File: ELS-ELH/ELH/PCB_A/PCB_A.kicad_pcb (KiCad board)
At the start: 2 copper layers, 95 x 95 mm, 40 parts, among them J1 Pressure Transducer Input, J2 Conn_01x09_Pin, J3 Conn_01x20_Pin, J4 Conn_01x20_Pin, Q1 IRLZ44N, Q2 IRLZ44N, Q4 IRLZ44N, Q6 IRLZ44N

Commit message: PCB B Advanced
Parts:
- J3, J4: footprint Connector_PinSocket_2.54mm:PinSocket_1x20_P2.54mm_Vertical -> Connector_PinHeader_2.54mm:PinHeader_1x20_P2.54mm_Vertical; moved to B.Cu
- moved J3 48.2 mm to (24.1, -40.0)
- moved J4 48.2 mm to (24.1, 40.0)

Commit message: Update of 3D Models
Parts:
- removed J1: Pressure Transducer Input, TerminalBlock:TerminalBlock_MaiXu_MX126-5.0-03P_1x03_P5.00mm
- removed J2: Conn_01x09_Pin, Connector_Hirose:Hirose_DF13-09P-1.25DSA_1x09_P1.25mm_Vertical
- J3, J4: footprint Connector_PinHeader_2.54mm:PinHeader_1x20_P2.54mm_Vertical -> Connector_PinSocket_2.54mm:PinSocket_1x20_P2.54mm_Vertical
- R1, R10, R11, R16, R18, R19, R2, R20, R3, R6, R8, R9: moved to B.Cu
- moved R20 100.5 mm to (-17.2, 2.55), turned to 180 degrees
- moved R18 100.5 mm to (-17.2, -5.55), turned to 180 degrees
- moved R19 100.5 mm to (-17.2, -1.50), turned to 180 degrees
- moved R10 85.8 mm to (25.8, -1.00), turned to 180 degrees
- moved R11 85.8 mm to (25.8, 3.05), turned to 180 degrees
- moved R9 85.8 mm to (25.8, -5.05), turned to 180 degrees
- moved C3 77.6 mm to (33.8, -35.0)
- moved C1 72.0 mm to (27.0, 17.5), turned to 90 degrees
- moved R16 58.8 mm to (10.0, 31.1), turned to 90 degrees
- moved R8 50.1 mm to (6.15, 23.2), turned to -90 degrees
- moved R6 45.8 mm to (2.10, 23.2), turned to -90 degrees
- moved R3 41.9 mm to (-1.95, 23.2), turned to -90 degrees
- moved R2 38.4 mm to (-6.00, 23.2), turned to -90 degrees
- moved R1 35.5 mm to (-10.1, 23.2), turned to -90 degrees
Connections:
- Regulator3 pad 3: Net-(Bornera2-Pin_1) -> GND
- Regulator3 pad 4: Net-(Bornera2-Pin_2) -> +5V

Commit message: advances
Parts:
- moved Bornera1 74.8 mm to (-33.5, -16.6), turned to -90 degrees
- moved Bornera7 67.8 mm to (33.5, -6.45), turned to 90 degrees
- moved R8 54.6 mm to (49.6, -9.95), turned to 0 degrees
- moved BOOST1 48.3 mm to (22.3, 37.8), turned to 180 degrees
- moved R16 37.0 mm to (-17.2, 6.00), turned to 180 degrees
- moved R1 34.1 mm to (-23.8, -8.00), turned to 0 degrees
- moved R19 33.1 mm to (-10.0, 30.8), turned to 90 degrees
- moved R6 31.9 mm to (17.9, -4.50), turned to 0 degrees
- moved R9 31.7 mm to (57.5, -6.50)
- moved R11 29.0 mm to (17.5, 30.8), turned to 90 degrees
- moved Bornera4 23.0 mm to (33.5, 16.6)
- moved R20 20.9 mm to (-14.0, 23.2), turned to -90 degrees
- moved R3 14.9 mm to (13.0, 23.2)
- moved D1 10.2 mm to (37.5, 21.5), turned to 180 degrees
- moved Q1 9.64 mm to (35.5, 26.5), turned to 180 degrees
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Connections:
- net /Ch_B_mosfet_1 renamed /Ch_C_mosfet_1
- R6 pad 1: /Ch_B_mosfet_2 -> /Ch_C_mosfet_2
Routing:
- net Net-(Bornera4-Pin_1): track 0.00 -> 80.4 mm
- net /Ch_D_mosfet_2: track 0.00 -> 62.5 mm
- net Net-(Bornera5-Pin_1): track 0.00 -> 44.9 mm
- net Net-(BOOST1-IN-): track 0.00 -> 43.9 mm
- net Net-(BOOST1-IN+): track 0.00 -> 41.0 mm
- net +12V: track 0.00 -> 40.9 mm
- net Net-(Q1-G): track 0.00 -> 36.9 mm
- net Net-(Bornera1-Pin_1): track 0.00 -> 35.9 mm
- net Net-(Bornera1-Pin_2): track 0.00 -> 35.1 mm
- net /Ch_C_mosfet_2: track 0.00 -> 32.5 mm
- net Net-(Q6-G): track 0.00 -> 31.1 mm
- net Net-(Q4-G): track 0.00 -> 18.9 mm
- net Net-(Q2-G): track 0.00 -> 16.9 mm
- net Net-(Q1-S): track 0.00 -> 9.05 mm
- net Net-(Q2-D): track 0.00 -> 6.49 mm

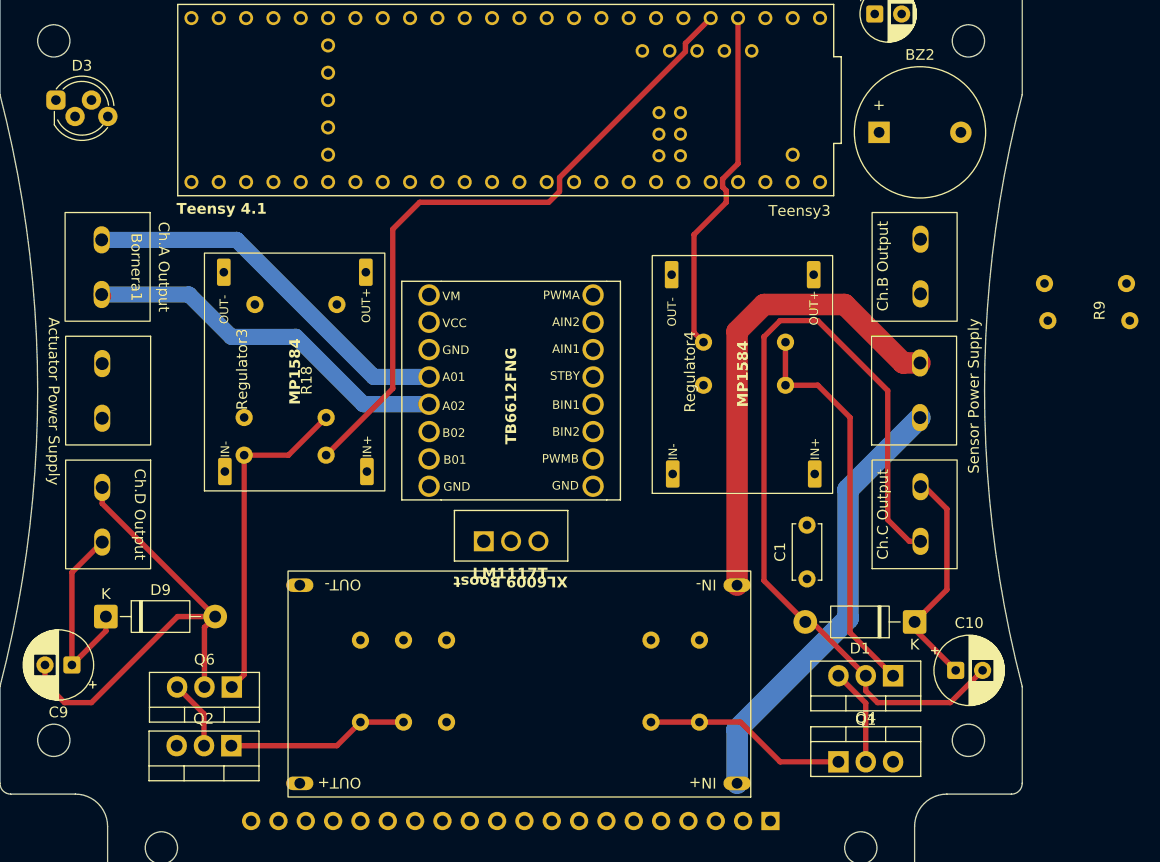
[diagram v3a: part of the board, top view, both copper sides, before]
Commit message: Updates
The boost component was replaced, capacitors were added for the regulator, and the power supply voltage for the expansion module was changed
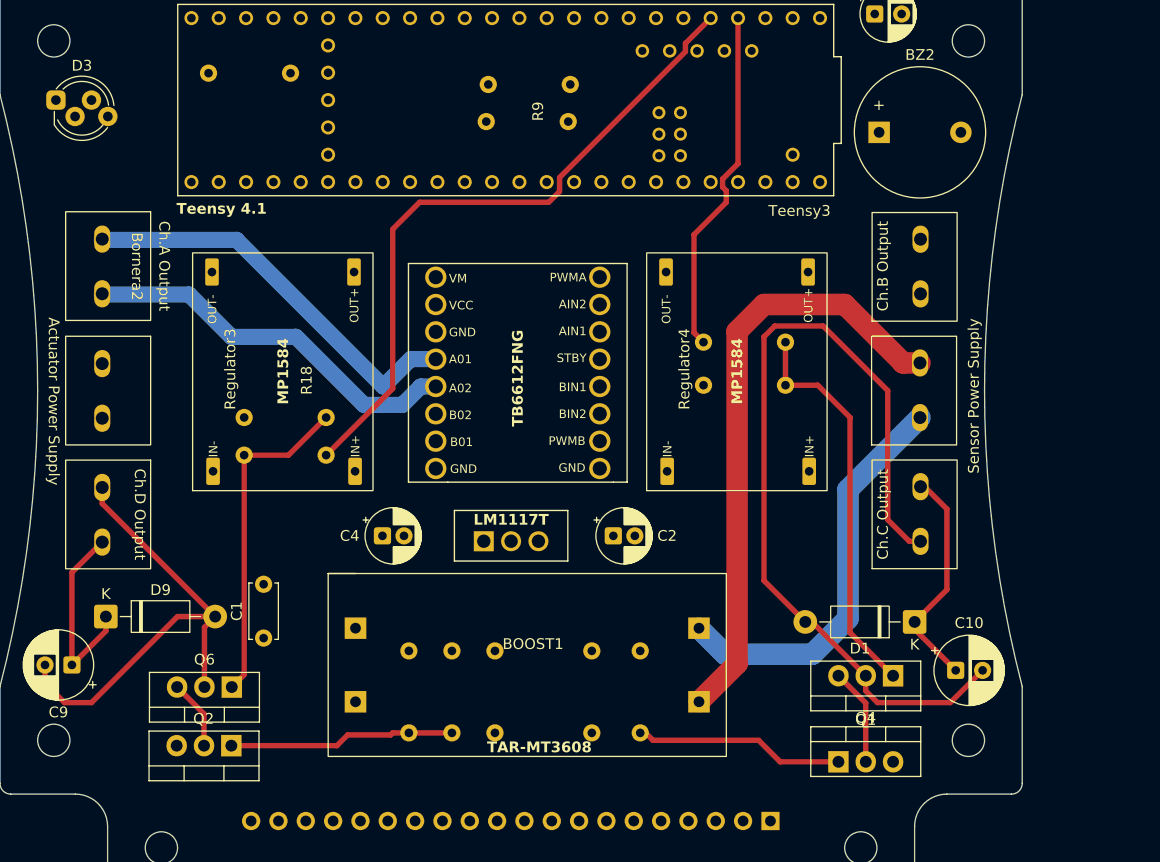
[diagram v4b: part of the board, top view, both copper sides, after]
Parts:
- removed Bornera1: Ch.A Output, ELH_Library:Bornera 2P
- added Bornera2: Ch.A Output, ELH_Library:Bornera 2P, F.Cu at (-33.5, -16.6)
- added C2: 10uF, Capacitor_THT:CP_Radial_D5.0mm_P2.00mm, F.Cu at (9.50, 13.5)
- added C4: 10uF, Capacitor_THT:CP_Radial_D5.0mm_P2.00mm, F.Cu at (-12.0, 13.5)
- BOOST1: value XL6009 -> TAR-MT3608; footprint ELH_Library:XL6009 Boost -> ELH_Library:TAR-MT3608
- moved R9 55.4 mm to (5.31, -25.0)
- moved R8 54.9 mm to (-2.12, -28.4)
- moved C1 50.8 mm to (-23.0, 23.0)
- moved BOOST1 44.4 mm to (-17.0, 17.0), turned to 0 degrees
- moved R1 21.9 mm to (-28.1, -29.5)
- moved R11 5.59 mm to (12.0, 31.8)
- moved R3 5.59 mm to (7.50, 24.2)
- moved R19 4.61 mm to (-5.50, 31.8)
- moved R2 4.61 mm to (-1.50, 24.2)
- moved R20 4.61 mm to (-9.50, 24.2)
- moved Driver_DC2 1.76 mm to (0.62, -1.65)
- moved Regulator3 1.10 mm to (-29.6, 9.30)
- moved Regulator4 0.57 mm to (12.6, 9.30)
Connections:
- Regulator1 pad 1: +5V -> GND
- Regulator1 pad 3: GND -> +5V
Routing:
- net Net-(BOOST1-IN-): track 43.9 -> 56.2 mm
- net Net-(Q2-G): track 16.9 -> 21.0 mm
- net Net-(BOOST1-IN+): track 41.0 -> 37.7 mm
- net Net-(Bornera2-Pin_1): track 35.9 -> 37.7 mm
- net Net-(Bornera2-Pin_2): track 35.1 -> 36.0 mm
- net Net-(Q4-G): track 18.9 -> 19.5 mm

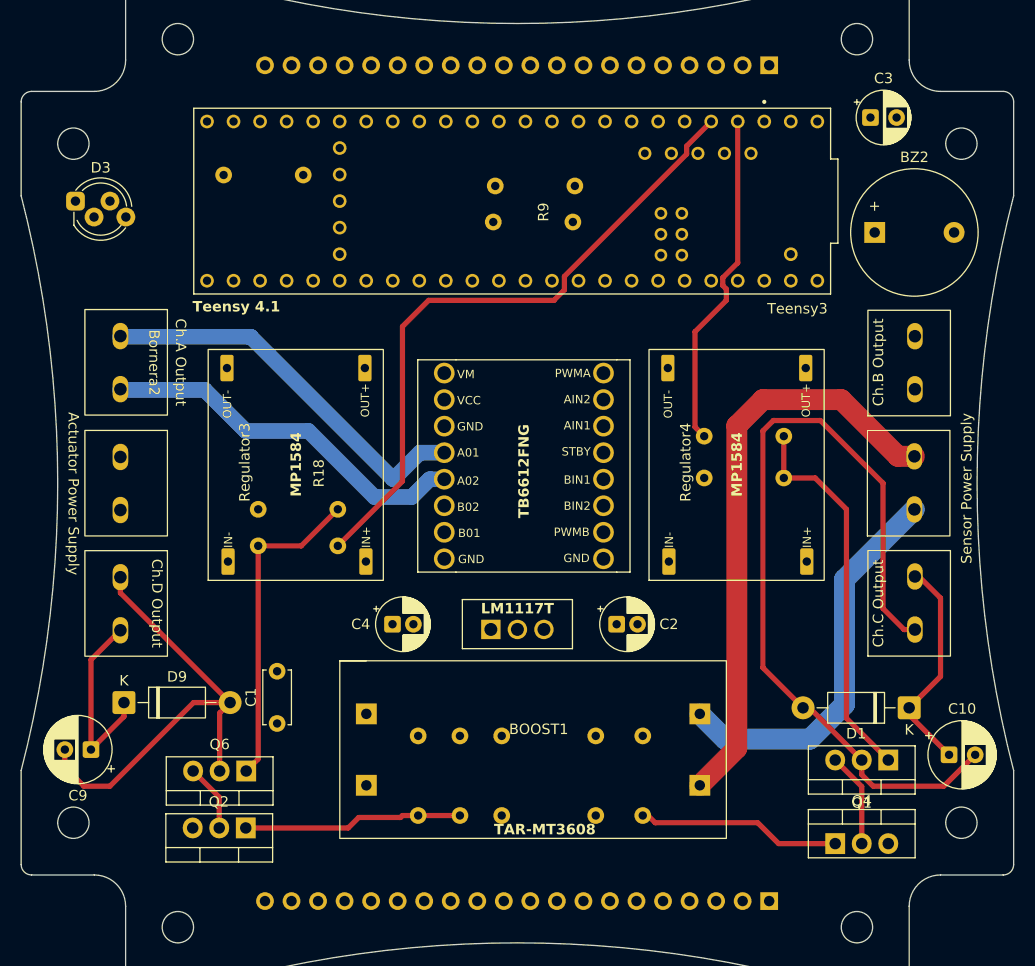
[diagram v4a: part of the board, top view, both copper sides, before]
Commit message: preliminary PCB A connections
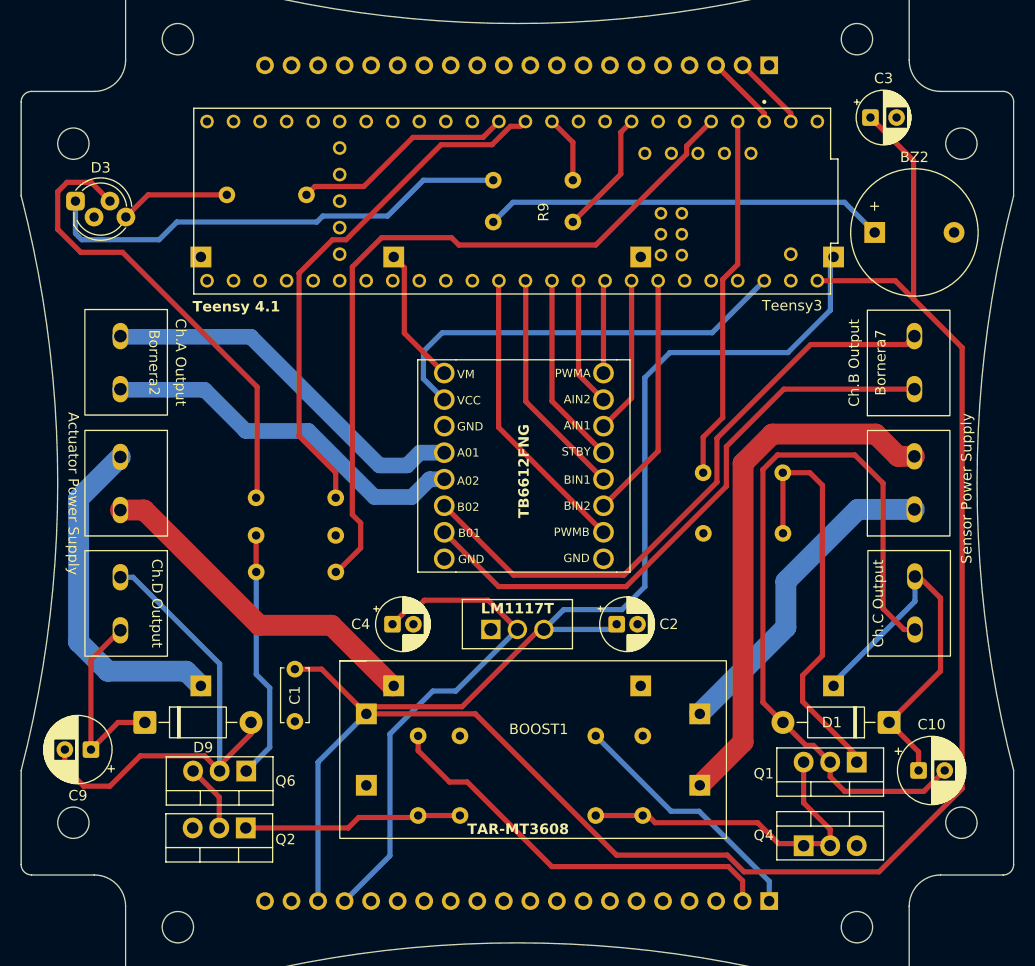
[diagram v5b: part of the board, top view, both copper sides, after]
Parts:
- Regulator3, Regulator4: value MP1584 -> LM2596; footprint ELH_Library:MP1584 -> ELH_Library:LM2596; moved to B.Cu
- moved Regulator3 62.2 mm to (31.5, 20.7)
- moved R2 32.7 mm to (-25.0, 1.40), turned to 0 degrees
- moved Regulator4 25.8 mm to (-10.6, 20.7)
- moved R18 8.21 mm to (-25.0, 5.00), turned to 0 degrees
- moved R10 5.30 mm to (25.4, 4.80)
- moved R6 3.50 mm to (17.8, -1.00)
- moved C10 3.28 mm to (38.4, 27.5)
- moved Q1 3.03 mm to (32.5, 26.7)
- moved Q4 3.03 mm to (27.4, 34.7)
- moved D9 2.76 mm to (-35.7, 22.9)
- moved R16 2.51 mm to (-17.4, 8.50)
- moved D1 2.38 mm to (35.6, 22.9)
- moved R1 1.93 mm to (-27.8, -27.6)
- moved C1 1.71 mm to (-21.3, 22.8)
- moved R8 0.58 mm to (-2.31, -29.0)
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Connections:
- J3 pad 1: unconnected-(J3-Pin_1-Pad1) -> GND
- J3 pad 2: unconnected-(J3-Pin_2-Pad2) -> /UART1_TX_1
- J3 pad 3: unconnected-(J3-Pin_3-Pad3) -> /UART1_RX_1
- J4 pad 1: unconnected-(J4-Pin_1-Pad1) -> /Ch_C_mosfet_1
- J4 pad 17: unconnected-(J4-Pin_17-Pad17) -> +3V3
- J4 pad 18: unconnected-(J4-Pin_18-Pad18) -> +5V
- J4 pad 2: unconnected-(J4-Pin_2-Pad2) -> /Ch_D_mosfet_1
- Teensy3 pad 14: /PWMA -> /PWMB
- Teensy3 pad 15: /AIN1 -> /BIN1
- Teensy3 pad 16: /AIN2 -> /STBY
- Teensy3 pad 17: /PWMB -> /AIN2
- Teensy3 pad 18: /BIN1 -> /PWMA
- Teensy3 pad 19: /BIN2 -> /AIN1
- Teensy3 pad 20: /STBY -> /BIN2
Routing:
- net +5V: track 0.00 -> 258.0 mm
- net Net-(Bornera7-Pin_2): track 0.00 -> 59.7 mm
- net Net-(Bornera7-Pin_1): track 0.00 -> 57.2 mm
- net /LED5: track 0.00 -> 50.6 mm
- net +3V3: track 0.00 -> 48.2 mm
- net Net-(D3-GA): track 0.00 -> 45.7 mm
- net Net-(D3-RA): track 0.00 -> 45.7 mm
- net +3.3VA: track 0.00 -> 40.9 mm
- net /Ch_D_mosfet_1: track 0.00 -> 39.6 mm
- net Net-(BZ2-+): track 0.00 -> 38.5 mm
- net Net-(Bornera3-Pin_1): track 0.00 -> 33.1 mm
- net Net-(Bornera3-Pin_2): track 0.00 -> 32.8 mm
- net /PWMB: track 0.00 -> 28.3 mm
- net +12V: track 40.9 -> 68.8 mm
- net /Ch_C_mosfet_1: track 0.00 -> 24.3 mm
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
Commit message: PCB A advances
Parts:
- added BOOST2: TAR-MT3608, ELH_Library:TAR-MT3608, F.Cu at (0.54, 21.1)
- added Bornera1: Camera Connection, ELH_Library:Bornera 2P, F.Cu at (-34.0, 8.10)
- added Bornera8: Camera Power Supply, ELH_Library:Bornera 2P, F.Cu at (33.7, -13.0)
- added J1: Conn_01x08_Pin, Connector_PinSocket_2.54mm:PinSocket_1x08_P2.54mm_Vertical, F.Cu at (-8.94, 9.70)
- J3, R9: moved to F.Cu
- moved C3 62.4 mm to (-24.3, -12.2)
- moved Regulator4 46.1 mm to (-32.5, -19.8), turned to -90 degrees
- moved C1 35.8 mm to (-13.3, -12.1), turned to 180 degrees
- moved D1 34.9 mm to (13.3, -3.90), turned to 0 degrees
- moved R6 34.7 mm to (20.1, 33.6), turned to 90 degrees
- moved C9 33.5 mm to (-14.8, 4.45)
- moved C4 33.0 mm to (21.0, 15.3), turned to 180 degrees
- moved Q2 31.6 mm to (-23.3, 1.50)
- moved R2 30.9 mm to (-26.1, -29.5)
- moved R9 30.8 mm to (30.9, -7.96), turned to -90 degrees
- moved C2 30.6 mm to (-21.0, 15.3), turned to 180 degrees
- moved Q4 28.3 mm to (15.8, 8.90)
- moved Q1 27.8 mm to (20.9, 1.50)
- moved D9 27.4 mm to (-30.1, -3.90)
- moved R16 25.0 mm to (-15.7, 33.5), turned to 90 degrees
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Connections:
- BOOST1 pad 2: Net-(BOOST1-IN-) -> GND
- Bornera3 pad 1: Net-(Bornera3-Pin_2) -> GND
- Bornera6 pad 2: Net-(BOOST1-IN-) -> GND
- Driver_DC2 pad 2: +3.3VA -> +3V3
- J3 pad 3: /UART1_RX_1 -> /UART1_TX_1
- J3 pad 4: unconnected-(J3-Pin_4-Pad4) -> /UART1_TX_1
- J3 pad 5: unconnected-(J3-Pin_5-Pad5) -> /UART1_RX_1
- J3 pad 6: unconnected-(J3-Pin_6-Pad6) -> /UART1_RX_1
- J3 pad 7: unconnected-(J3-Pin_7-Pad7) -> /UART1_RX_1
- J4 pad 1: /Ch_C_mosfet_1 -> unconnected-(J4-Pin_1-Pad1)
- J4 pad 13: unconnected-(J4-Pin_13-Pad13) -> +3V3
- J4 pad 14: unconnected-(J4-Pin_14-Pad14) -> +5V
- J4 pad 17: +3V3 -> unconnected-(J4-Pin_17-Pad17)
- J4 pad 18: +5V -> /Ch_D_mosfet_1
- J4 pad 19: unconnected-(J4-Pin_19-Pad19) -> /Ch_D_mosfet_1
- J4 pad 2: /Ch_D_mosfet_1 -> unconnected-(J4-Pin_2-Pad2)
- J4 pad 20: unconnected-(J4-Pin_20-Pad20) -> /Ch_D_mosfet_1
- J4 pad 7: unconnected-(J4-Pin_7-Pad7) -> /Ch_C_mosfet_1
- J4 pad 8: unconnected-(J4-Pin_8-Pad8) -> /Ch_C_mosfet_1
- J4 pad 9: unconnected-(J4-Pin_9-Pad9) -> /Ch_C_mosfet_1
- Regulator4 pad 1: Net-(Bornera3-Pin_2) -> GND
- Teensy3 pad 1: /UART1_RX_1 -> unconnected-(Teensy3-TX1-Pad1)
- Teensy3 pad 11: /LED6 -> /LED4
- Teensy3 pad 13: unconnected-(Teensy3-SCK-Pad13) -> /LPWM
- Teensy3 pad 2: /Ch_C_mosfet_2 -> unconnected-(Teensy3-OUT2-Pad2)
- Teensy3 pad 22: unconnected-(Teensy3-A8-Pad22) -> /Ch_C_mosfet_2
- Teensy3 pad 3: /Ch_D_mosfet_2 -> unconnected-(Teensy3-LRCLK2-Pad3)
- Teensy3 pad 3.3V_1: +3.3VA -> +3V3
- Teensy3 pad 3.3V_2: +3.3VA -> +3V3
- Teensy3 pad 36: unconnected-(Teensy3-CS2-Pad36) -> /Ch_D_mosfet_2
- Teensy3 pad 4: unconnected-(Teensy3-BCLK2-Pad4) -> /UART1_RX_1
- Teensy3 pad 41: unconnected-(Teensy3-A17-Pad41) -> /RPWM
- Teensy3 pad 9: /LED4 -> /LED6
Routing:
- net +3V3: track 48.2 -> 253.5 mm
- net +12V: track 68.8 -> 252.4 mm
- net +5V: track 258.0 -> 161.4 mm
- net Net-(BOOST2-OUT+): track 0.00 -> 58.8 mm
- net Net-(BOOST1-IN-): track 51.0 -> 0.00 mm
- net Net-(BOOST2-IN+): track 0.00 -> 44.7 mm
- net +3.3VA: track 40.9 -> 0.00 mm
- net /RPWM: track 0.00 -> 39.3 mm
- net Net-(Bornera4-Pin_1): track 73.9 -> 36.2 mm
- net /LPWM: track 0.00 -> 37.0 mm
- net /BUZZER2: track 11.9 -> 48.8 mm
- net Net-(BOOST1-IN+): track 31.3 -> 68.0 mm
- net Net-(D3-GA): track 45.7 -> 11.0 mm
- net Net-(Bornera3-Pin_2): track 32.8 -> 0.00 mm
- net Net-(D3-RA): track 45.7 -> 14.1 mm
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- added copper zone on B.Cu, net GND
- added copper zone on F.Cu, net GND
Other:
- outline, holes or cut-outs redrawn
- board text added: "B01"
- board text added: "BIN1"

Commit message: PCB B connection advances
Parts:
- J3: moved to B.Cu
- moved J3 48.2 mm to (-24.1, -44.0)
- moved D3 0.24 mm to (-38.5, -33.3)
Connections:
- J3 pad 1: GND -> unconnected-(J3-Pin_1-Pad1)
- J3 pad 14: unconnected-(J3-Pin_14-Pad14) -> /UART1_RX_1
- J3 pad 15: unconnected-(J3-Pin_15-Pad15) -> /UART1_RX_1
- J3 pad 16: unconnected-(J3-Pin_16-Pad16) -> /UART1_RX_1
- J3 pad 17: unconnected-(J3-Pin_17-Pad17) -> /UART1_TX_1
- J3 pad 18: unconnected-(J3-Pin_18-Pad18) -> /UART1_TX_1
- J3 pad 19: unconnected-(J3-Pin_19-Pad19) -> /UART1_TX_1
- J3 pad 2: /UART1_TX_1 -> unconnected-(J3-Pin_2-Pad2)
- J3 pad 20: unconnected-(J3-Pin_20-Pad20) -> GND
- J3 pad 3: /UART1_TX_1 -> unconnected-(J3-Pin_3-Pad3)
- J3 pad 4: /UART1_TX_1 -> unconnected-(J3-Pin_4-Pad4)
- J3 pad 5: /UART1_RX_1 -> unconnected-(J3-Pin_5-Pad5)
- J3 pad 6: /UART1_RX_1 -> unconnected-(J3-Pin_6-Pad6)
- J3 pad 7: /UART1_RX_1 -> unconnected-(J3-Pin_7-Pad7)
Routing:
- net +5V: track 161.4 -> 272.6 mm
- net Net-(BOOST2-IN+): track 44.7 -> 44.0 mm
